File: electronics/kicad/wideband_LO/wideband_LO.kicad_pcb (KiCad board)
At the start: 2 copper layers, 27 parts, among them U1 BFP620

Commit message: Various sims
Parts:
- moved C1 2.25 mm to (93.2, 103.9)
- moved C2 2.25 mm to (93.5, 96.7)
- moved C3 2.25 mm to (99.3, 105.4)
- moved C4 2.25 mm to (101.3, 98.2)
- moved C5 2.25 mm to (96.8, 99.2)
- moved C6 2.25 mm to (99.0, 91.6)
- moved D1 2.25 mm to (89.6, 96.7)
- moved D2 2.25 mm to (91.6, 96.7)
- moved D3 2.25 mm to (96.7, 101.2)
- moved D4 2.25 mm to (96.7, 103.2)
- moved L1 2.25 mm to (87.6, 96.7)
- moved L2 2.25 mm to (98.8, 101.2)
- moved L3 2.25 mm to (98.8, 99.2)
- moved L4 2.25 mm to (96.8, 95.6)
- moved L5 2.25 mm to (96.8, 93.6)
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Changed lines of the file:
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@@
     (visible_elements FFFFFF7F)
     (pcbplotparams
-      (layerselection 0x010fc_ffffffff)
+      (layerselection 0x00000_7fffffff)
       (usegerberextensions false)
       (usegerberattributes false)
@@
       (creategerberjobfile false)
       (excludeedgelayer true)
-      (linewidth 0.010000)
+      (linewidth 0.020000)
       (plotframeref false)
       (viasonmask false)
       (mode 1)
-      (useauxorigin false)
+      (useauxorigin true)
       (hpglpennumber 1)
       (hpglpenspeed 20)
@@
       (outputformat 1)
       (mirror false)
-      (drillshape 1)
+      (drillshape 0)
       (scaleselection 1)
-      (outputdirectory ""))
+      (outputdirectory "CAM/"))
   )
   (net 0 "")
@@
   )
   (module Capacitors:0402 (layer F.Cu)
-    (at 107.8 99.2 90)
+    (at 105.55 99.2 90)
     (descr "GENERIC 1005 (0402) PACKAGE")
     (tags "GENERIC 1005 (0402) PACKAGE")
@@
   )
   (module Capacitors:0402 (layer F.Cu)
-    (at 97.8 100.2 180)
+    (at 95.55 100.2 180)
     (descr "GENERIC 1005 (0402) PACKAGE")
     (tags "GENERIC 1005 (0402) PACKAGE")
@@
   )
   (module Capacitors:0402 (layer F.Cu)
-    (at 94.75 95.25 270)
+    (at 92.5 95.25 270)
     (descr "GENERIC 1005 (0402) PACKAGE")
     (tags "GENERIC 1005 (0402) PACKAGE")
@@
   )
   (module Capacitors:0402 (layer F.Cu)
-    (at 97.8 102.2)
+    (at 95.55 102.2)
     (descr "GENERIC 1005 (0402) PACKAGE")
     (tags "GENERIC 1005 (0402) PACKAGE")
@@
   )
   (module Capacitors:0402 (layer F.Cu)
-    (at 96.35 95.25 270)
+    (at 94.1 95.25 270)
     (descr "GENERIC 1005 (0402) PACKAGE")
     (tags "GENERIC 1005 (0402) PACKAGE")
@@
   )
   (module Capacitors:0402 (layer F.Cu)
-    (at 92.75 98 90)
+    (at 90.5 98 90)
     (descr "GENERIC 1005 (0402) PACKAGE")
     (tags "GENERIC 1005 (0402) PACKAGE")
@@
   )
   (module Capacitors:0402 (layer F.Cu)
-    (at 99 105.2 270)
+    (at 96.75 105.2 270)
     (descr "GENERIC 1005 (0402) PACKAGE")
     (tags "GENERIC 1005 (0402) PACKAGE")
@@
   )
   (module Capacitors:0402 (layer F.Cu)
-    (at 99 93.6 90)
+    (at 96.75 93.6 90)
     (descr "GENERIC 1005 (0402) PACKAGE")
     (tags "GENERIC 1005 (0402) PACKAGE")
@@
   )
   (module Capacitors:0402 (layer F.Cu)
-    (at 99 95.57912 90)
+    (at 96.75 95.57912 90)
     (descr "GENERIC 1005 (0402) PACKAGE")
     (tags "GENERIC 1005 (0402) PACKAGE")
@@
   )
   (module Capacitors:0402 (layer F.Cu)
-    (at 101 99.2 90)
+    (at 98.75 99.2 90)
     (descr "GENERIC 1005 (0402) PACKAGE")
     (tags "GENERIC 1005 (0402) PACKAGE")
@@
   )
   (module Capacitors:0402 (layer F.Cu)
-    (at 101 101.2 90)
+    (at 98.75 101.2 90)
     (descr "GENERIC 1005 (0402) PACKAGE")
     (tags "GENERIC 1005 (0402) PACKAGE")
@@
   )
   (module Capacitors:0402 (layer F.Cu)
-    (at 89.85 96.7 180)
+    (at 87.6 96.7 180)
     (descr "GENERIC 1005 (0402) PACKAGE")
     (tags "GENERIC 1005 (0402) PACKAGE")
@@
   )
   (module Capacitors:0603 (layer F.Cu)
-    (at 101.25 91.6 180)
+    (at 99 91.6 180)
     (descr "GENERIC 1608 (0603) PACKAGE")
     (tags "GENERIC 1608 (0603) PACKAGE")
@@
   )
   (module Capacitors:0402 (layer F.Cu)
-    (at 99 99.22088 90)
+    (at 96.75 99.22088 90)
     (descr "GENERIC 1005 (0402) PACKAGE")
     (tags "GENERIC 1005 (0402) PACKAGE")
@@
   )
   (module Capacitors:0402 (layer F.Cu)
-    (at 103.6 98.2)
+    (at 101.35 98.2)
     (descr "GENERIC 1005 (0402) PACKAGE")
     (tags "GENERIC 1005 (0402) PACKAGE")
@@
   )
   (module Capacitors:0603 (layer F.Cu)
-    (at 101.6 105.4 90)
+    (at 99.35 105.4 90)
     (descr "GENERIC 1608 (0603) PACKAGE")
     (tags "GENERIC 1608 (0603) PACKAGE")
@@
   )
   (module Capacitors:0402 (layer F.Cu)
-    (at 95.75 96.65 180)
+    (at 93.5 96.65 180)
     (descr "GENERIC 1005 (0402) PACKAGE")
     (tags "GENERIC 1005 (0402) PACKAGE")
@@
   )
   (module Capacitors:0603 (layer F.Cu)
-    (at 95.4 103.90164 90)
+    (at 93.15 103.90164 90)
     (descr "GENERIC 1608 (0603) PACKAGE")
     (tags "GENERIC 1608 (0603) PACKAGE")
@@
   )
   (module TestPoint:TestPoint_Pad_1.5x1.5mm (layer F.Cu)
-    (at 93.4 102)
+    (at 91.15 102)
     (descr "SMD rectangular pad as test Point, square 1.5mm side length")
     (tags "test point SMD pad rectangle square")
@@
   )
   (module Diode_SMD:D_SOD-523 (layer F.Cu)
-    (at 93.847057 96.717156)
+    (at 91.597057 96.717156)
     (descr "http://www.diodes.com/datasheets/ap02001.pdf p.144")
     (tags "Diode SOD523")
@@
   )
   (module Diode_SMD:D_SOD-523 (layer F.Cu)
-    (at 98.95 101.2 90)
+    (at 96.7 101.2 90)
     (descr "http://www.diodes.com/datasheets/ap02001.pdf p.144")
     (tags "Diode SOD523")
@@
   )
   (module Diode_SMD:D_SOD-523 (layer F.Cu)
-    (at 91.85 96.717157 180)
+    (at 89.6 96.717157 180)
     (descr "http://www.diodes.com/datasheets/ap02001.pdf p.144")
     (tags "Diode SOD523")
@@
   )
   (module Diode_SMD:D_SOD-523 (layer F.Cu)
-    (at 98.95 103.199999 270)
+    (at 96.7 103.199999 270)
     (descr "http://www.diodes.com/datasheets/ap02001.pdf p.144")
     (tags "Diode SOD523")
@@
   )
   (module Package_TO_SOT_SMD:SOT-343_SC-70-4 (layer F.Cu)
-    (at 98 97.4)
+    (at 95.75 97.4)
     (descr "SOT-343, SC-70-4")
     (tags "SOT-343 SC-70-4")
@@
   )
   (module TestPoint:TestPoint_Pad_2.0x2.0mm (layer F.Cu)
-    (at 99 91.6)
+    (at 96.75 91.6)
     (descr "SMD rectangular pad as test Point, square 2.0mm side length")
     (tags "test point SMD pad rectangle square")
@@
   )
   (module TestPoint:TestPoint_Pad_2.0x2.0mm (layer F.Cu)
-    (at 101.6 103.2)
+    (at 99.35 103.2)
     (descr "SMD rectangular pad as test Point, square 2.0mm side length")
     (tags "test point SMD pad rectangle square")
@@
   )
   (module TestPoint:TestPoint_Pad_1.5x1.5mm (layer F.Cu)
-    (at 107.8 98.2)
+    (at 105.55 98.2)
     (descr "SMD rectangular pad as test Point, square 1.5mm side length")
     (tags "test point SMD pad rectangle square")
@@
       (net 15 noutput))
   )
-  (segment (start 87.75 107.75) (end 107.25 107.75) (width 1) (layer F.Cu) (net 1))
-  (segment (start 95.35164 102) (end 95.4 102.04836) (width 1) (layer F.Cu) (net 14))
-  (segment (start 93.4 102) (end 95.35164 102) (width 1) (layer F.Cu) (net 14))
-  (segment (start 95.55164 102.2) (end 95.4 102.04836) (width 1) (layer F.Cu) (net 14))
-  (segment (start 97 102.2) (end 95.33076 102.2) (width 1) (layer F.Cu) (net 14))
-  (segment (start 93.4 102) (end 93.4 99.65) (width 1) (layer F.Cu) (net 14))
-  (segment (start 93.4 99.65) (end 92.75 99) (width 1) (layer F.Cu) (net 14))
-  (segment (start 107.8 101.2033) (end 107.75 101.2533) (width 1) (layer F.Cu) (net 1))
-  (segment (start 107.8 100.07582) (end 107.8 101.5) (width 1) (layer F.Cu) (net 1))
-  (segment (start 107.4 98.2) (end 105 98.2) (width 1.5) (layer F.Cu) (net 15))
-  (segment (start 98.8 98.2) (end 99.49958 98.2) (width 1.5) (layer F.Cu) (net 4))
-  (segment (start 103.22088 98.2) (end 102.5467 98.2) (width 0.25) (layer F.Cu) (net 4))
-  (segment (start 102.2 98.2) (end 99.6533 98.2) (width 1.5) (layer F.Cu) (net 4))
+  (segment (start 85.5 107.75) (end 105 107.75) (width 1) (layer F.Cu) (net 1))
+  (segment (start 93.10164 102) (end 93.15 102.04836) (width 1) (layer F.Cu) (net 14))
+  (segment (start 91.15 102) (end 93.10164 102) (width 1) (layer F.Cu) (net 14))
+  (segment (start 93.30164 102.2) (end 93.15 102.04836) (width 1) (layer F.Cu) (net 14))
+  (segment (start 94.75 102.2) (end 93.08076 102.2) (width 1) (layer F.Cu) (net 14))
+  (segment (start 91.15 102) (end 91.15 99.65) (width 1) (layer F.Cu) (net 14))
+  (segment (start 91.15 99.65) (end 90.5 99) (width 1) (layer F.Cu) (net 14))
+  (segment (start 105.55 101.2033) (end 105.5 101.2533) (width 1) (layer F.Cu) (net 1))
+  (segment (start 105.55 100.07582) (end 105.55 101.5) (width 1) (layer F.Cu) (net 1))
+  (segment (start 105.15 98.2) (end 102.75 98.2) (width 1.5) (layer F.Cu) (net 15))
+  (segment (start 96.55 98.2) (end 97.24958 98.2) (width 1.5) (layer F.Cu) (net 4))
+  (segment (start 100.97088 98.2) (end 100.2967 98.2) (width 0.25) (layer F.Cu) (net 4))
+  (segment (start 99.95 98.2) (end 97.4033 98.2) (width 1.5) (layer F.Cu) (net 4))
   (zone (net 1) (net_name GND) (layer F.Cu) (hatch edge 0.508)
     (connect_pads (clearance 2))
@@
     (polygon
       (pts
-        (xy 108.75 109.25) (xy 86 109.25) (xy 86 85.75) (xy 108.75 85.75)
+        (xy 106.5 109.25) (xy 83.75 109.25) (xy 83.75 85.75) (xy 106.5 85.75)
       )
     )
@@
     (polygon
       (pts
-        (xy 106.25 109.25) (xy 93 109.25) (xy 93 105.75) (xy 106.25 105.75)
+        (xy 104 109.25) (xy 90.75 109.25) (xy 90.75 105.75) (xy 104 105.75)
       )
     )
@@
     (polygon
       (pts
-        (xy 107.25 95) (xy 101.75 95) (xy 101.75 88)
+        (xy 105 95) (xy 99.5 95) (xy 99.5 88)
       )
     )
@@
     (polygon
       (pts
-        (xy 89.5 99.25) (xy 86.5 99.25) (xy 89.5 91.75)
+        (xy 87.25 99.25) (xy 84.25 99.25) (xy 87.25 91.75)
       )
     )
@@
     (polygon
       (pts
-        (xy 96.75 94.75) (xy 93.25 94.75) (xy 93.25 92) (xy 96.75 88.75)
+        (xy 94.5 94.75) (xy 91 94.75) (xy 91 92) (xy 94.5 88.75)
       )
     )

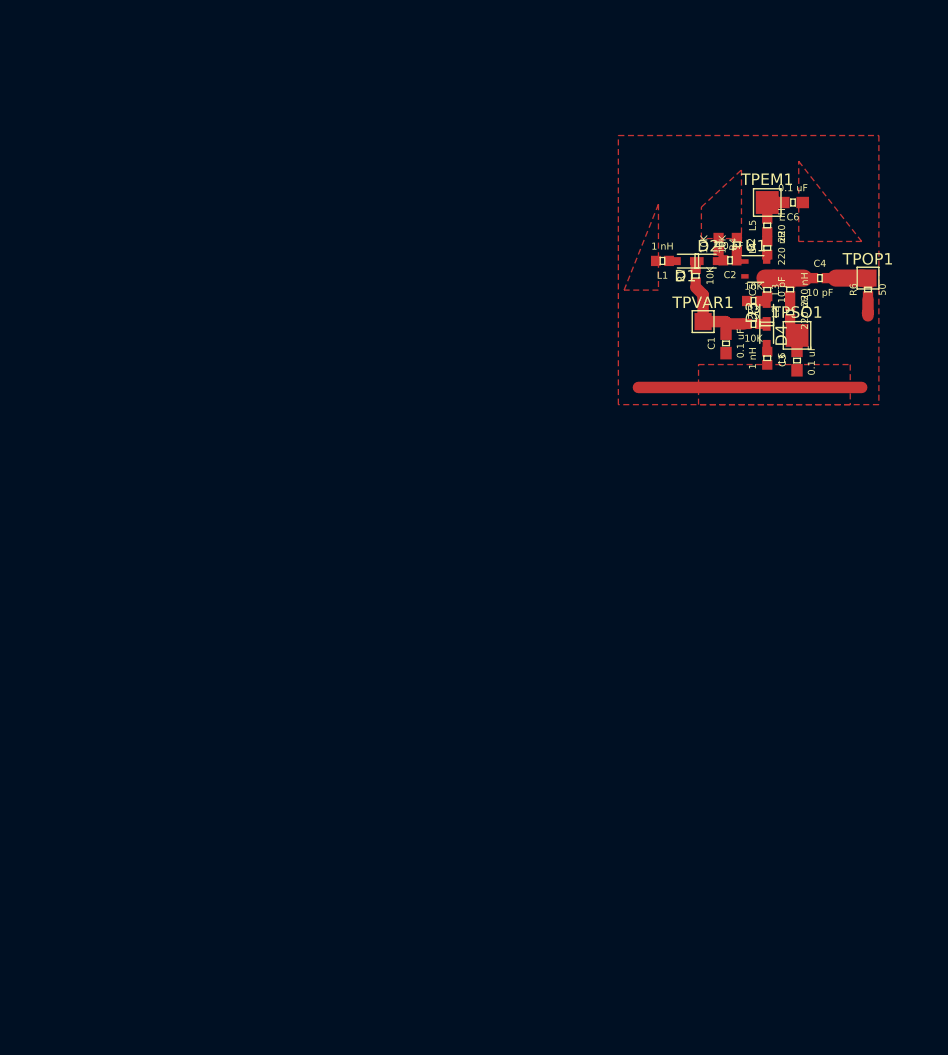
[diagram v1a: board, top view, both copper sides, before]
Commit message: Reduced pad size, found bug with FDTD, etc, etc.
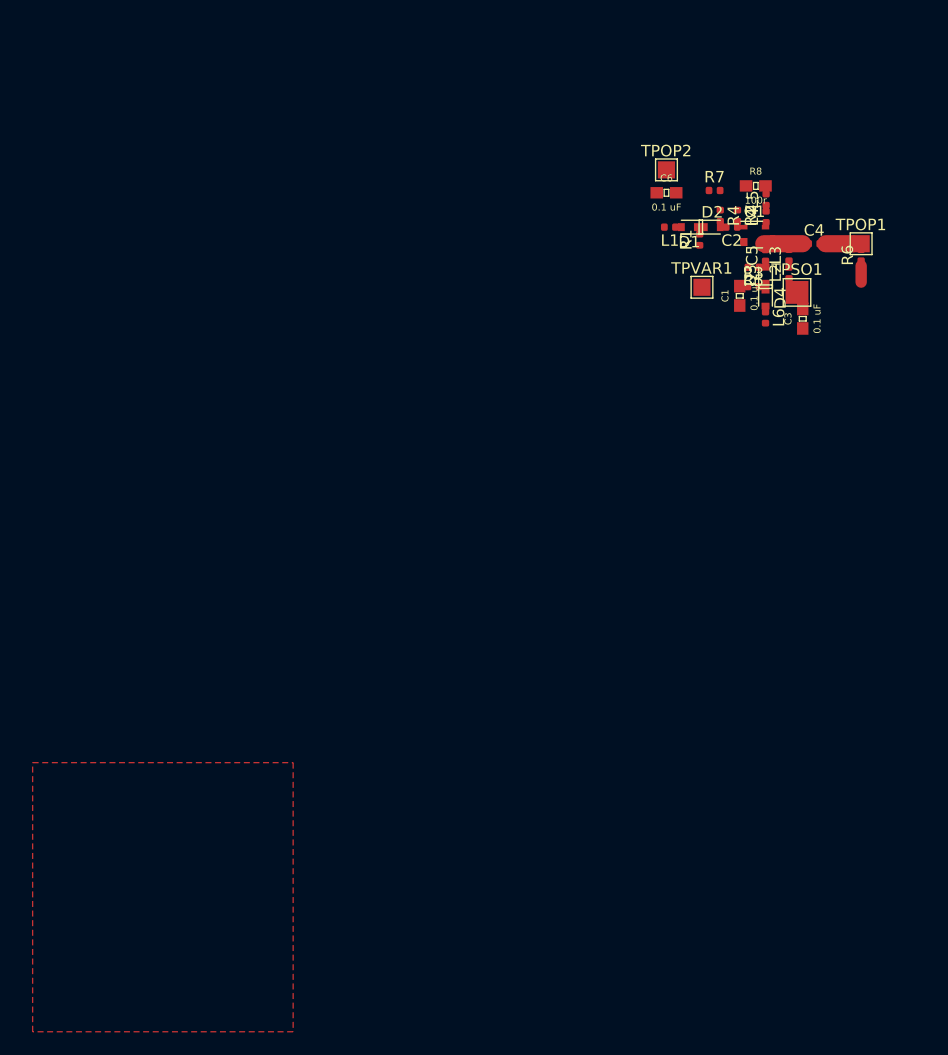
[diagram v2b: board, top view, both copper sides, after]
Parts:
- removed TPEM1: Vemitter, TestPoint:TestPoint_Pad_2.0x2.0mm
- added R7: 10K, Resistor_SMD:R_0402_1005Metric, F.Cu at (92.2, 90.5)
- added R8: 100r, Capacitors:0603, F.Cu at (95.8, 90.2)
- added TPOP2: Voutput, TestPoint:TestPoint_Pad_1.5x1.5mm, F.Cu at (88.0, 88.8)
- C2, C4, C5: footprint Capacitors:0402 -> Capacitor_SMD:C_0402_1005Metric
- L1, L2, L3, L4, L5, L6, R1, R2, R3, R4, R5, R6: footprint Capacitors:0402 -> Resistor_SMD:R_0402_1005Metric
- moved C6 11.1 mm to (88.0, 90.8), turned to 0 degrees
- moved C1 4.32 mm to (94.3, 99.8)
- moved TPSO1 3.75 mm to (99.3, 99.5)
- moved C3 3.68 mm to (99.8, 101.8)
- moved L6 3.55 mm to (96.6, 101.7)
- moved L2 3.45 mm to (98.7, 97.8)
- moved D3 3.25 mm to (96.6, 98.0)
- moved D4 3.25 mm to (96.6, 100.0)
- moved R3 3.25 mm to (95.5, 99.0)
- moved R1 3.17 mm to (90.8, 94.8)
- moved R6 3.06 mm to (105.0, 96.2)
- moved TPOP1 3.06 mm to (105.0, 95.2)
- moved C4 3.04 mm to (100.8, 95.2)
- moved L1 3.02 mm to (88.2, 93.8)
- moved C5 3.00 mm to (96.6, 96.2)
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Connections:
- C6 pad 1: GND -> Net-(C6-Pad1)
- C6 pad 2: nemitter -> GND
- L5 pad 2: nemitter -> Net-(L5-Pad2)
- R2 pad 1: GND -> Net-(C6-Pad1)
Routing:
- net GND: track 21.0 -> 1.42 mm
- net nvaractor: track 7.17 -> 0.00 mm
- net Net-(C4-Pad1): track 3.92 -> 3.25 mm

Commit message: Buck-boost to linear
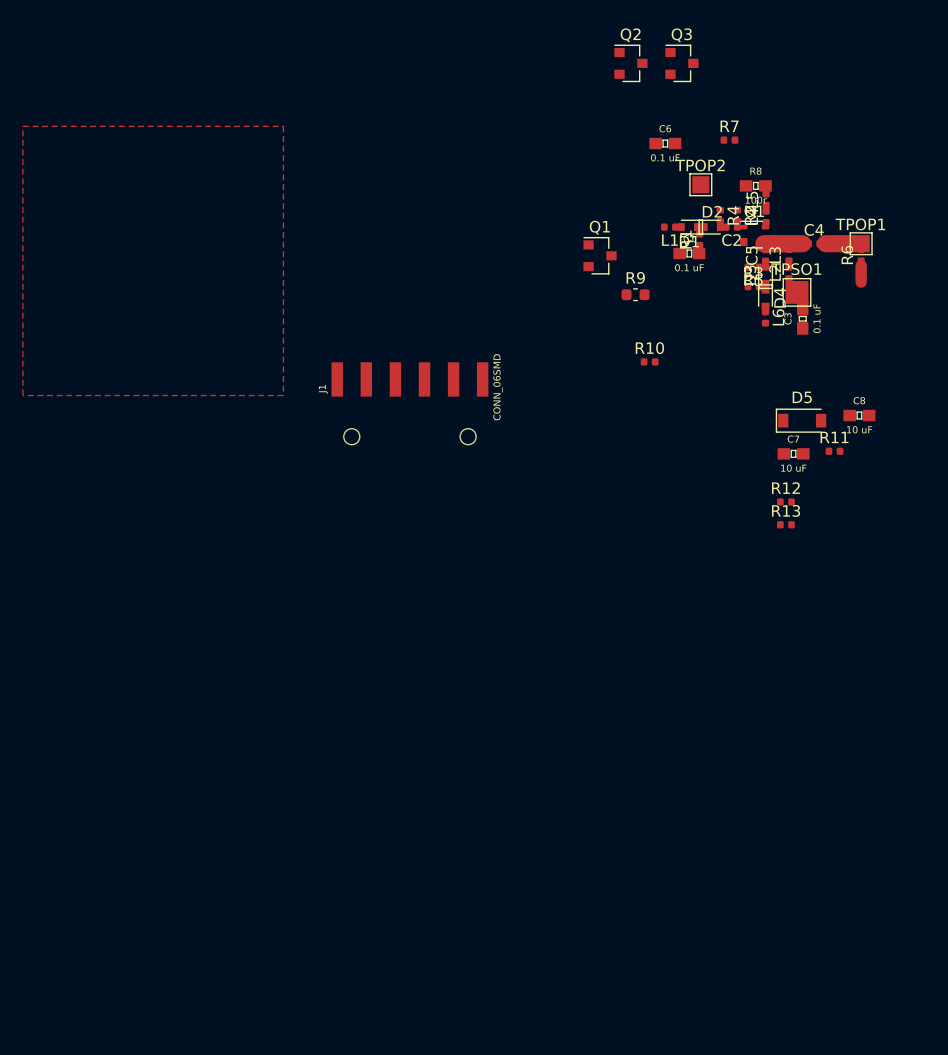
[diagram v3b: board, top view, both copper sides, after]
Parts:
- removed TPVAR1: , TestPoint:TestPoint_Pad_1.5x1.5mm
- added C7: 10 uF, Capacitors:0603, F.Cu at (99.0, 113.5)
- added C8: 10 uF, Capacitors:0603, F.Cu at (104.8, 110.2)
- added D5: D, Diode_SMD:D_SOD-123, F.Cu at (99.8, 110.7)
- added J1: CONN_06SMD, Connectors2:1X06-SMD_RA_MALE, F.Cu at (65.5, 112.0)
- added Q1: 2N7002, Package_TO_SOT_SMD:SOT-23, F.Cu at (82.2, 96.2)
- added Q2: BSS84, Package_TO_SOT_SMD:SOT-23, F.Cu at (84.8, 79.5)
- added Q3: BSS84, Package_TO_SOT_SMD:SOT-23, F.Cu at (89.3, 79.5)
- added R10: 10K, Resistor_SMD:R_0402_1005Metric, F.Cu at (86.5, 105.5)
- added R11: 30k, Resistor_SMD:R_0402_1005Metric, F.Cu at (102.6, 113.3)
- added R12: 1k, Resistor_SMD:R_0402_1005Metric, F.Cu at (98.4, 117.8)
- added R13: 30k, Resistor_SMD:R_0402_1005Metric, F.Cu at (98.4, 119.7)
- added R9: 10k, Resistor_SMD:R_0603_1608Metric, F.Cu at (85.2, 99.7)
- TPOP2: value Voutput -> Vbias
- moved C1 5.75 mm to (90.0, 96.0), turned to 0 degrees
- moved R7 4.59 mm to (93.5, 86.2)
- moved C6 4.30 mm to (87.8, 86.5)
- moved TPOP2 3.27 mm to (91.0, 90.0)
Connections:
- C1 pad 2: nvaractor -> Net-(C1-Pad2)

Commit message: Backup
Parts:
- removed C1: 0.1 uF, Capacitors:0603
- removed C7, C8: 10 uF, Capacitors:0603
- removed D5: D, Diode_SMD:D_SOD-123
- removed J1: CONN_06SMD, Connectors2:1X06-SMD_RA_MALE
- removed Q1: 2N7002, Package_TO_SOT_SMD:SOT-23
- removed Q2, Q3: BSS84, Package_TO_SOT_SMD:SOT-23
- removed R10: 10K, Resistor_SMD:R_0402_1005Metric
- removed R11, R13: 30k, Resistor_SMD:R_0402_1005Metric
- removed R12: 1k, Resistor_SMD:R_0402_1005Metric
- removed R9: 10k, Resistor_SMD:R_0603_1608Metric
- added C11: 0.1 uF, Capacitors:0603, F.Cu at (90.0, 100.8)
- added TPOP9: varactor, TestPoint:TestPoint_Pad_1.5x1.5mm, F.Cu at (92.1, 100.7)
- C6: value 0.1 uF -> 10 uF
- moved C3 10.8 mm to (100.0, 91.0), turned to 270 degrees
- moved C6 9.41 mm to (94.6, 93.0), turned to 180 degrees
- moved TPSO1 6.89 mm to (100.8, 92.7), turned to 180 degrees
- moved R7 5.36 mm to (93.1, 91.5)
- moved R5 3.82 mm to (99.0, 99.0), turned to 0 degrees
- moved L2 3.58 mm to (99.9, 94.4), turned to 270 degrees
- moved R8 2.31 mm to (97.9, 91.0), turned to 270 degrees
- moved C2 2.15 mm to (94.9, 95.5)
- moved C4 2.15 mm to (102.1, 97.0)
- moved C5 2.15 mm to (97.8, 98.0)
- moved D1 2.15 mm to (91.2, 95.5)
- moved D2 2.15 mm to (93.2, 95.5)
- moved D3 2.15 mm to (97.8, 99.7)
- moved D4 2.15 mm to (97.8, 101.7)
- moved L1 2.15 mm to (89.5, 95.5)
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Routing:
- net GND: track 1.42 -> 13.2 mm
- net nvaractor: track 0.00 -> 7.83 mm
- net Net-(C6-Pad1): track 0.00 -> 4.12 mm
- added copper zone on F.Cu, net nsource
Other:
- net class Default: trace_width 0.2 -> 0.5

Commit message: Driver card
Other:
- board outline added: 23.2 x 21.5 mm
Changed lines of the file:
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@@
   (general
     (thickness 1.6)
-    (drawings 0)
+    (drawings 4)
     (tracks 18)
     (zones 0)
@@
   (setup
     (last_trace_width 0.5)
+    (user_trace_width 0.2)
     (trace_clearance 0.2)
     (zone_clearance 0.1)
@@
       (net 15 noutput))
   )
+  (gr_line (start 83.75 107.25) (end 83.75 85.75) (layer Edge.Cuts) (width 0.05))
+  (gr_line (start 106.95 107.25) (end 83.75 107.25) (layer Edge.Cuts) (width 0.05))
+  (gr_line (start 106.95 85.75) (end 106.95 107.25) (layer Edge.Cuts) (width 0.05))
+  (gr_line (start 83.75 85.75) (end 106.95 85.75) (layer Edge.Cuts) (width 0.05))
   (segment (start 106.2 98.87582) (end 106.2 100.3) (width 1) (layer F.Cu) (net 1))
   (segment (start 89.015 93.015) (end 89.015 95.5) (width 0.5) (layer F.Cu) (net 1))
